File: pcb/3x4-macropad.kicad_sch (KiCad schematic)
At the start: 48 parts, among them SW1 SW_Push, SW10 SW_Push, SW11 SW_Push, SW12 SW_Push, SW2 SW_Push, SW3 SW_Push, SW4 SW_Push, SW5 SW_Push, SW6 SW_Push, SW7 SW_Push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

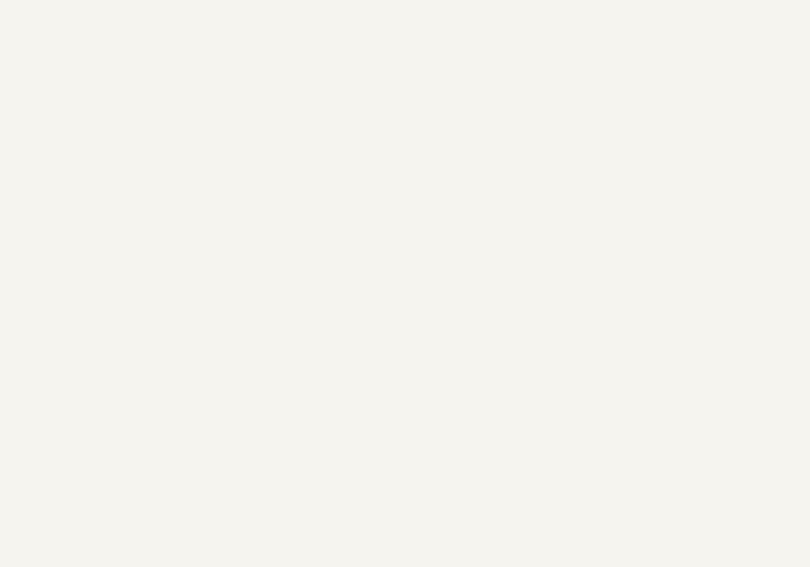
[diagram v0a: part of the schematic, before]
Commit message: V0.2 changed to gasket mount, added plate file, modified pcb to fix bugs
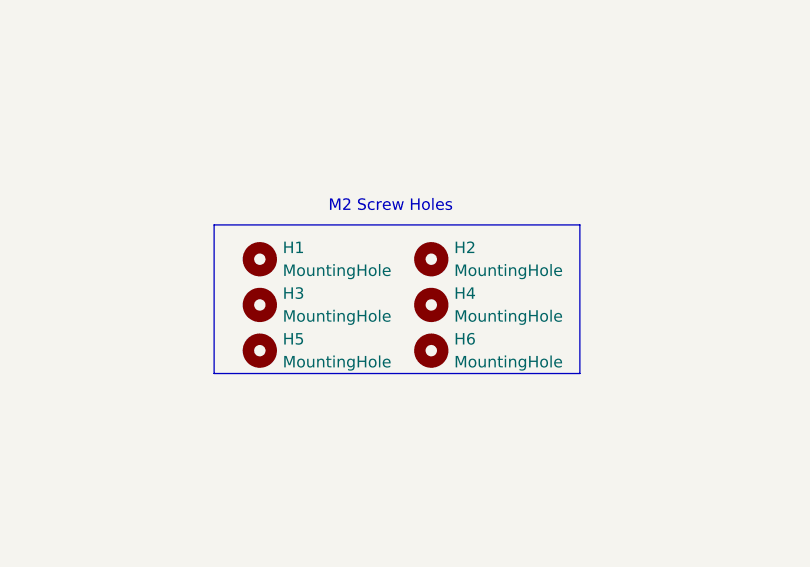
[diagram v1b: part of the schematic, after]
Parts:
- added H1, H2, H3, H4, H5, H6: MountingHole, MountingHole:MountingHole_2.2mm_M2_DIN965_Pad_TopBottom, symbol Mechanical:MountingHole
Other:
- note added: "M2 Screw Holes"
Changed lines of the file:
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@@
+    (fill (type none))
+  )
+  (rectangle (start 234.95 105.41) (end 275.59 121.92)
+    (stroke (width 0) (type default))
     (fill (type none))
   )
@@
   )
   (text "Pull-up resistors for proper I2C operation" (at 60.96 111.76 0)
+    (effects (font (size 1.27 1.27)) (justify left bottom))
+  )
+  (text "M2 Screw Holes" (at 247.65 104.14 0)
     (effects (font (size 1.27 1.27)) (justify left bottom))
   )
@@
         (path "/4718bde0-6351-4659-a829-1991d59f7064"
           (reference "LED2") (unit 1)
+        )
+      )
+    )
+  )
+  (symbol (lib_id "Mechanical:MountingHole") (at 240.03 119.38 0) (unit 1)
+    (in_bom yes) (on_board yes) (dnp no) (fields_autoplaced)
+    (property "Reference" "H5" (at 242.57 118.11 0)
+      (effects (font (size 1.27 1.27)) (justify left))
+    )
+    (property "Value" "MountingHole" (at 242.57 120.65 0)
+      (effects (font (size 1.27 1.27)) (justify left))
+    )
+    (property "Footprint" "MountingHole:MountingHole_2.2mm_M2_DIN965_Pad_TopBottom" (at 240.03 119.38 0)
+      (effects (font (size 1.27 1.27)) hide)
+    )
+    (property "Datasheet" "~" (at 240.03 119.38 0)
+      (effects (font (size 1.27 1.27)) hide)
+    )
+    (instances
+      (project "3x4-macropad"
+        (path "/4718bde0-6351-4659-a829-1991d59f7064"
+          (reference "H5") (unit 1)
         )
       )
@@
     )
   )
+  (symbol (lib_id "Mechanical:MountingHole") (at 259.08 109.22 0) (unit 1)
+    (in_bom yes) (on_board yes) (dnp no) (fields_autoplaced)
+    (property "Reference" "H2" (at 261.62 107.95 0)
+      (effects (font (size 1.27 1.27)) (justify left))
+    )
+    (property "Value" "MountingHole" (at 261.62 110.49 0)
+      (effects (font (size 1.27 1.27)) (justify left))
+    )
+    (property "Footprint" "MountingHole:MountingHole_2.2mm_M2_DIN965_Pad_TopBottom" (at 259.08 109.22 0)
+      (effects (font (size 1.27 1.27)) hide)
+    )
+    (property "Datasheet" "~" (at 259.08 109.22 0)
+      (effects (font (size 1.27 1.27)) hide)
+    )
+    (instances
+      (project "3x4-macropad"
+        (path "/4718bde0-6351-4659-a829-1991d59f7064"
+          (reference "H2") (unit 1)
+        )
+      )
+    )
+  )
   (symbol (lib_id "Diode:1N4148") (at 265.43 199.39 180) (unit 1)
     (in_bom yes) (on_board yes) (dnp no)
@@
     )
   )
+  (symbol (lib_id "Mechanical:MountingHole") (at 259.08 119.38 0) (unit 1)
+    (in_bom yes) (on_board yes) (dnp no) (fields_autoplaced)
+    (property "Reference" "H6" (at 261.62 118.11 0)
+      (effects (font (size 1.27 1.27)) (justify left))
+    )
+    (property "Value" "MountingHole" (at 261.62 120.65 0)
+      (effects (font (size 1.27 1.27)) (justify left))
+    )
+    (property "Footprint" "MountingHole:MountingHole_2.2mm_M2_DIN965_Pad_TopBottom" (at 259.08 119.38 0)
+      (effects (font (size 1.27 1.27)) hide)
+    )
+    (property "Datasheet" "~" (at 259.08 119.38 0)
+      (effects (font (size 1.27 1.27)) hide)
+    )
+    (instances
+      (project "3x4-macropad"
+        (path "/4718bde0-6351-4659-a829-1991d59f7064"
+          (reference "H6") (unit 1)
+        )
+      )
+    )
+  )
+  (symbol (lib_id "Mechanical:MountingHole") (at 240.03 109.22 0) (unit 1)
+    (in_bom yes) (on_board yes) (dnp no) (fields_autoplaced)
+    (property "Reference" "H1" (at 242.57 107.95 0)
+      (effects (font (size 1.27 1.27)) (justify left))
+    )
+    (property "Value" "MountingHole" (at 242.57 110.49 0)
+      (effects (font (size 1.27 1.27)) (justify left))
+    )
+    (property "Footprint" "MountingHole:MountingHole_2.2mm_M2_DIN965_Pad_TopBottom" (at 240.03 109.22 0)
+      (effects (font (size 1.27 1.27)) hide)
+    )
+    (property "Datasheet" "~" (at 240.03 109.22 0)
+      (effects (font (size 1.27 1.27)) hide)
+    )
+    (instances
+      (project "3x4-macropad"
+        (path "/4718bde0-6351-4659-a829-1991d59f7064"
+          (reference "H1") (unit 1)
+        )
+      )
+    )
+  )
   (symbol (lib_id "Diode:1N4148") (at 207.01 92.71 90) (mirror x) (unit 1)
     (in_bom yes) (on_board yes) (dnp no)
@@
         (path "/4718bde0-6351-4659-a829-1991d59f7064"
           (reference "#PWR035") (unit 1)
+        )
+      )
+    )
+  )
+  (symbol (lib_id "Mechanical:MountingHole") (at 259.08 114.3 0) (unit 1)
+    (in_bom yes) (on_board yes) (dnp no) (fields_autoplaced)
+    (property "Reference" "H4" (at 261.62 113.03 0)
+      (effects (font (size 1.27 1.27)) (justify left))
+    )
+    (property "Value" "MountingHole" (at 261.62 115.57 0)
+      (effects (font (size 1.27 1.27)) (justify left))
+    )
+    (property "Footprint" "MountingHole:MountingHole_2.2mm_M2_DIN965_Pad_TopBottom" (at 259.08 114.3 0)
+      (effects (font (size 1.27 1.27)) hide)
+    )
+    (property "Datasheet" "~" (at 259.08 114.3 0)
+      (effects (font (size 1.27 1.27)) hide)
+    )
+    (instances
+      (project "3x4-macropad"
+        (path "/4718bde0-6351-4659-a829-1991d59f7064"
+          (reference "H4") (unit 1)
         )
       )
@@
         )
       )
+    )
+  )
+  (symbol (lib_id "Mechanical:MountingHole") (at 240.03 114.3 0) (unit 1)
+    (in_bom yes) (on_board yes) (dnp no) (fields_autoplaced)
+    (property "Reference" "H3" (at 242.57 113.03 0)
+      (effects (font (size 1.27 1.27)) (justify left))
+    )
+    (property "Value" "MountingHole" (at 242.57 115.57 0)
+      (effects (font (size 1.27 1.27)) (justify left))
+    )
+    (property "Footprint" "MountingHole:MountingHole_2.2mm_M2_DIN965_Pad_TopBottom" (at 240.03 114.3 0)
+      (effects (font (size 1.27 1.27)) hide)
+    )
+    (property "Datasheet" "~" (at 240.03 114.3 0)
+      (effects (font (size 1.27 1.27)) hide)
+    )
+    (instances
+      (project "3x4-macropad"
+        (path "/4718bde0-6351-4659-a829-1991d59f7064"
+          (reference "H3") (unit 1)
+        )
+      )
